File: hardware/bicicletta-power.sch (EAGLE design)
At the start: 19 parts, among them IC1 LM5017, IC2 LM1117-3.3

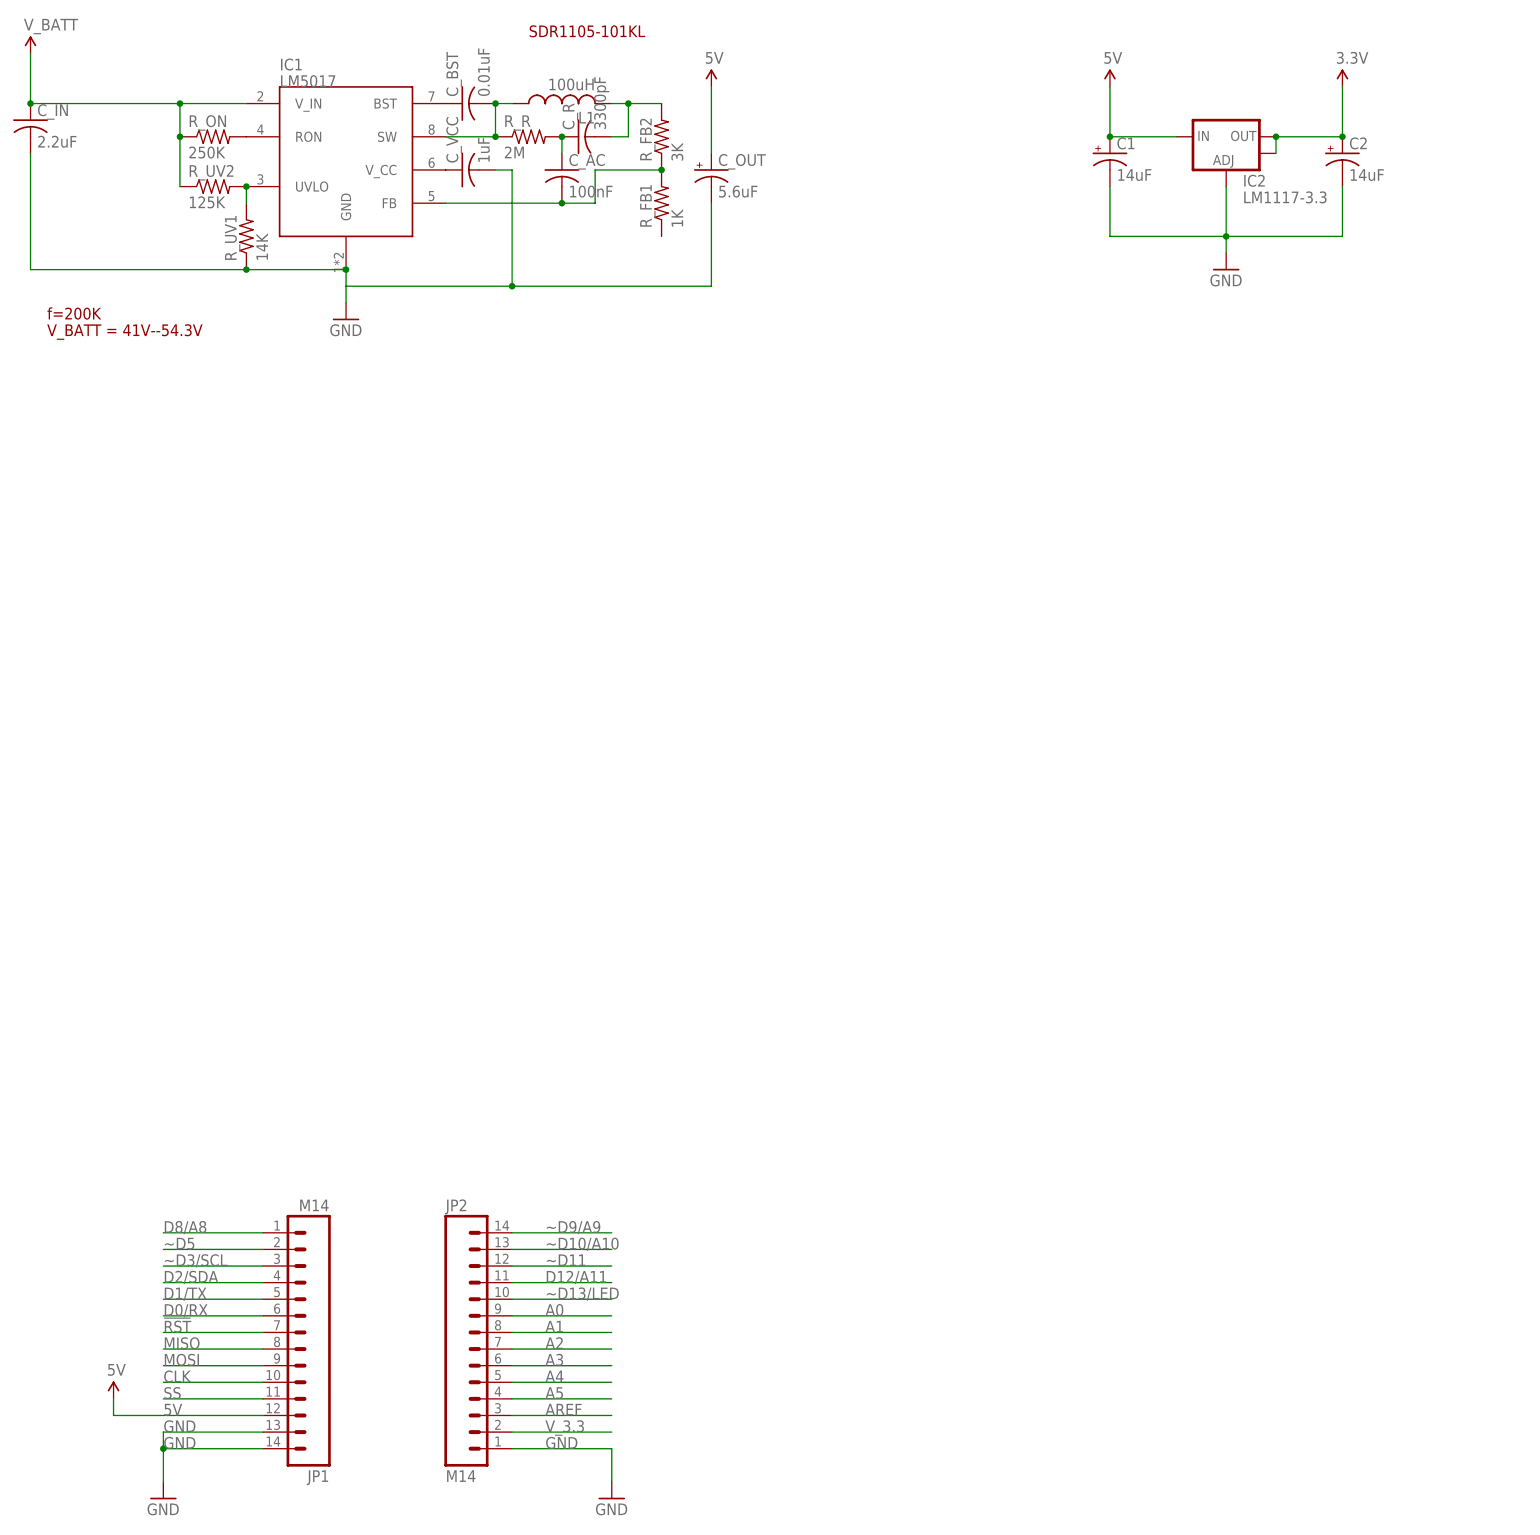
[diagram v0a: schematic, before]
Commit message: Adding connectors.
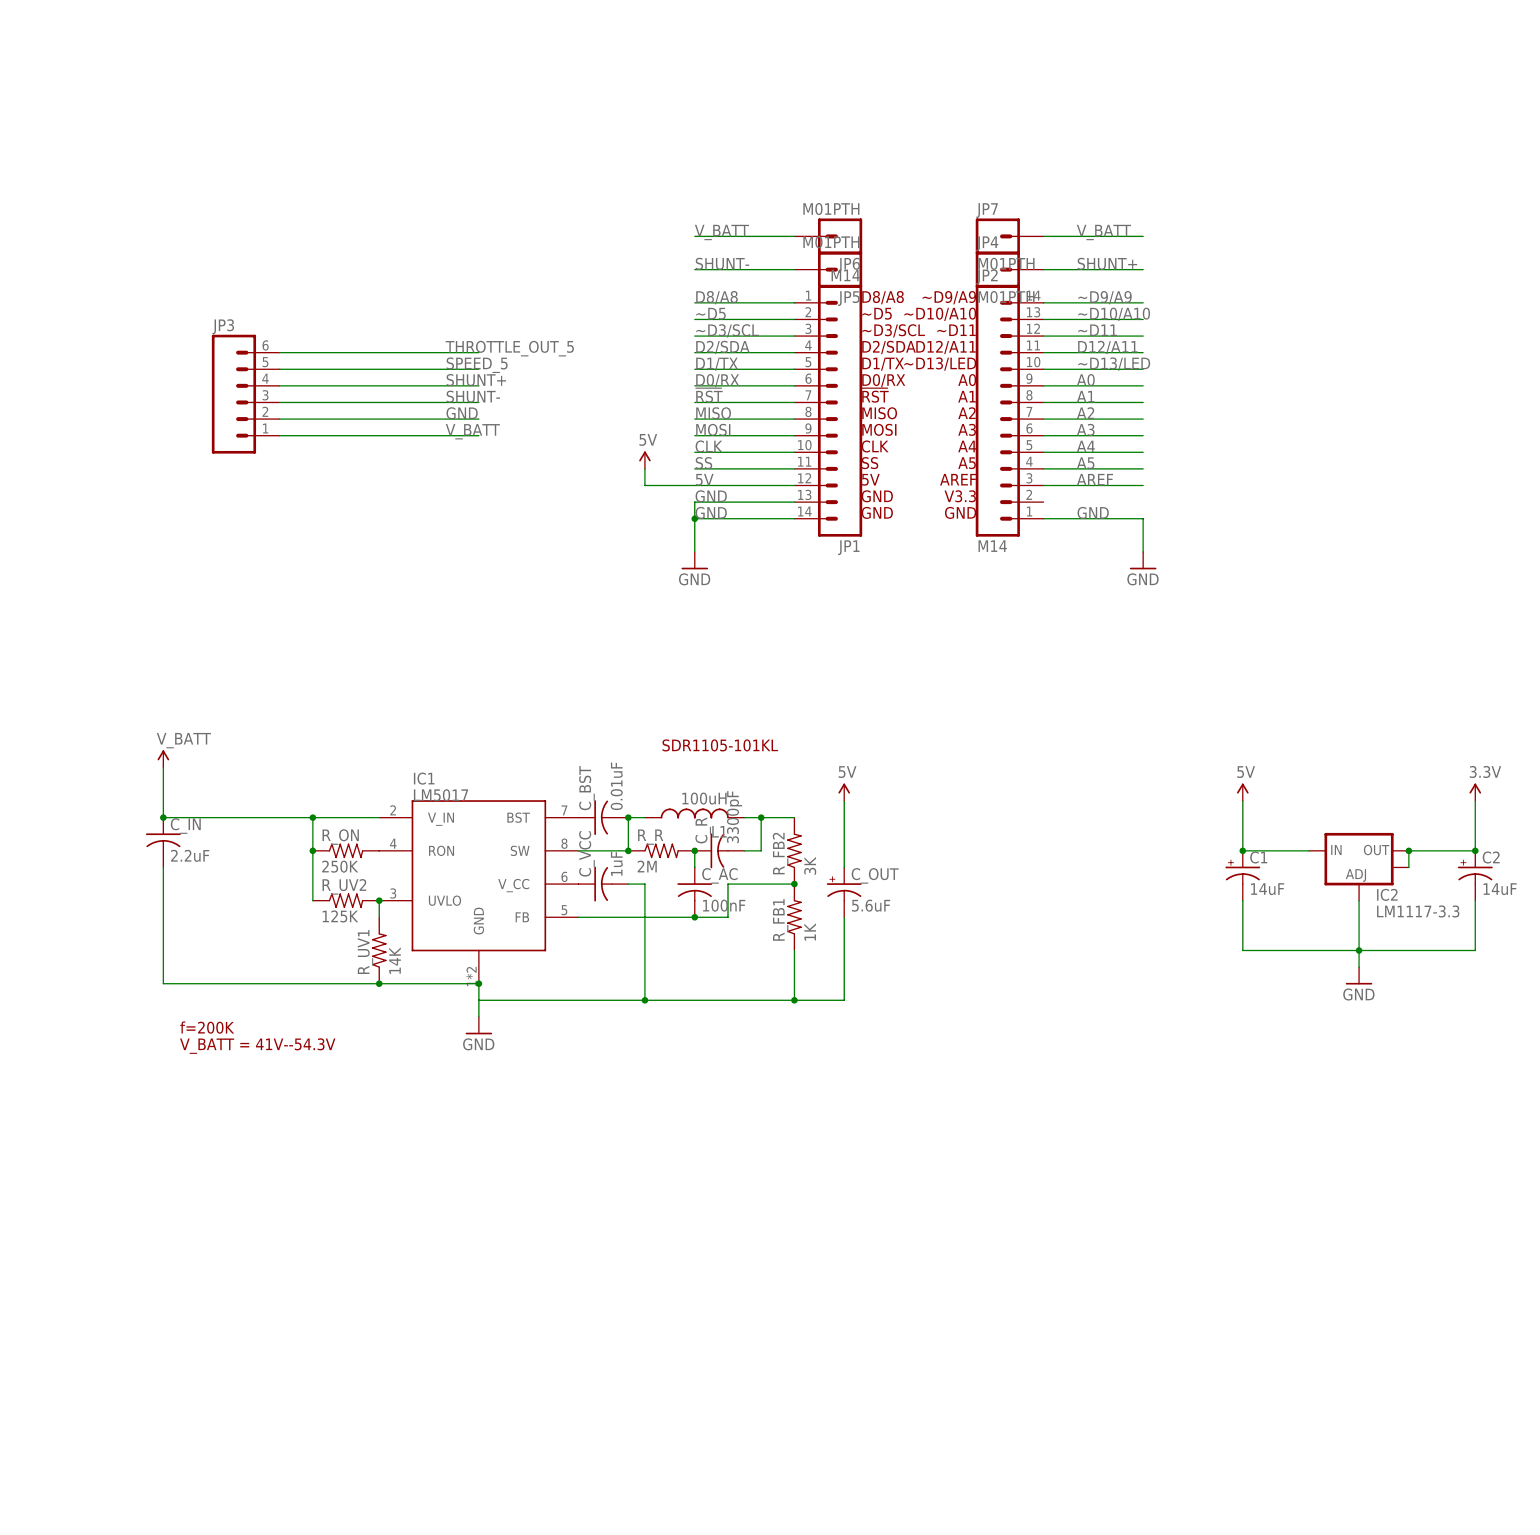
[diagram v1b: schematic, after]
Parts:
- added JP3: (no value), SparkFun-Connectors:M06LONGPADS
- added JP4, JP5, JP6, JP7: M01PTH, SparkFun-Connectors:M01PTH
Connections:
- removed net V_3.3: JP2.2
- new net SHUNT+: JP3.4, JP4.1
- new net SHUNT-: JP3.3
- new net SPEED_5: JP3.5
- new net THROTTLE_OUT_5: JP3.6
- net GND: now also JP3.2, R_FB1.1
- net V_BATT: now also JP3.1, JP6.1, JP7.1
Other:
- note added: "!RST"
- note added: "5V"
- note added: "A0"
- note added: "A1"
- note added: "A2"
- note added: "A3"
- note added: "A4"
- note added: "A5"
- note added: "AREF"
- note added: "CLK"
- note added: "D0/RX"
- note added: "D1/TX"
- note added: "D12/A11"
- note added: "D2/SDA"
- note added: "D8/A8"
- note added: "GND"
- note added: "MISO"
- note added: "MOSI"
- note added: "SS"
- note added: "V3.3"
- note added: "~D10/A10"
- note added: "~D11"
- note added: "~D13/LED"
- note added: "~D3/SCL"
- note added: "~D5"
- note added: "~D9/A9"
- moved on the sheet: C1, C2, C_AC, C_BST, C_IN, C_OUT, C_R, C_VCC, IC1, IC2, JP1, JP2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

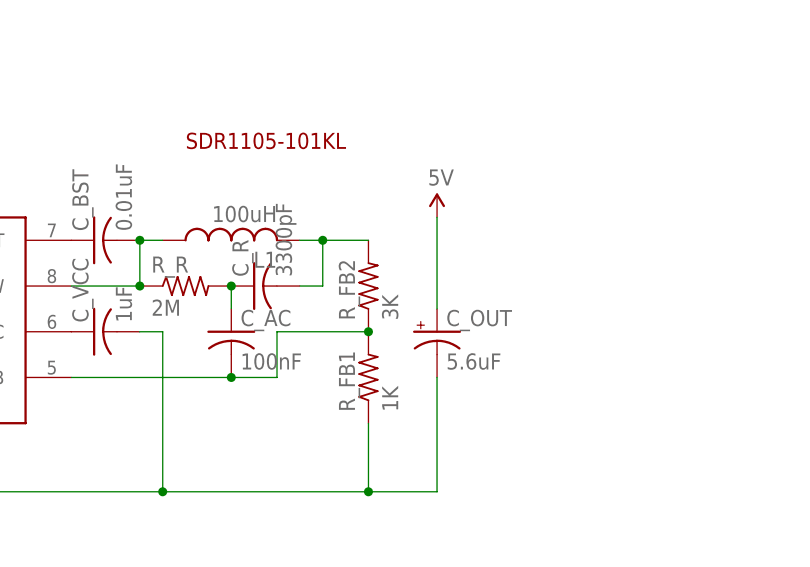
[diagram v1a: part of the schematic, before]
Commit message: Error in regulator connections. Please double check
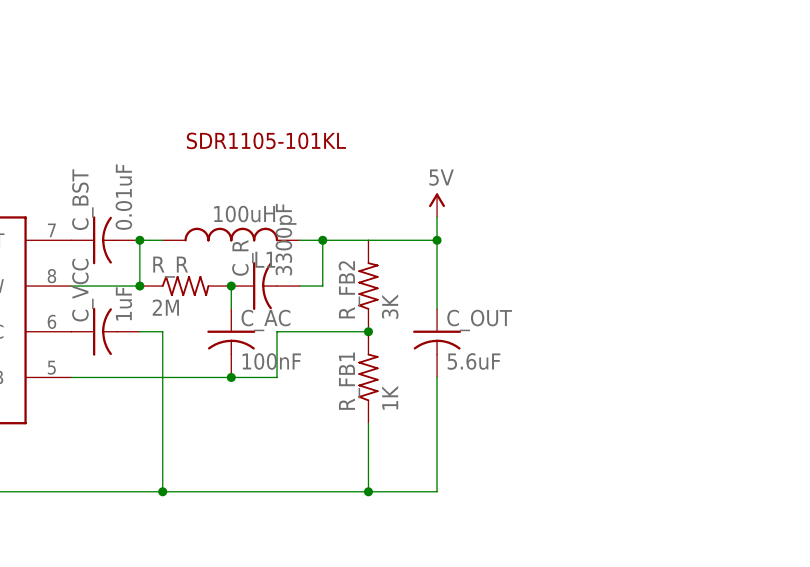
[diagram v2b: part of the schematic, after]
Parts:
- C_OUT: device rcl:CPOL-USUD-5X5,8 -> rcl:C-USC0603
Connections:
- removed net N$5: C_R.2, L1.2, R_FB2.2
- net 5V: now also C_OUT.1, C_R.2, L1.2, R_FB2.2; no longer C_OUT.+
- net GND: now also C_OUT.2; no longer C_OUT.-
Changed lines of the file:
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@@
 <part name="C_BST" library="rcl" deviceset="C-US" device="C0603" value="0.01uF"/>
 <part name="C_IN" library="rcl" deviceset="C-US" device="C1210K" value="2.2uF"/>
-<part name="C_OUT" library="rcl" deviceset="CPOL-US" device="UD-5X5,8" value="5.6uF"/>
+<part name="C_OUT" library="rcl" deviceset="C-US" device="C0603" value="5.6uF"/>
 <part name="R_UV2" library="rcl" deviceset="R-US_" device="M0805" value="125K"/>
 <part name="R_UV1" library="rcl" deviceset="R-US_" device="M0805" value="14K"/>
@@
 <pinref part="R_UV1" gate="G$1" pin="1"/>
 <junction x="60.96" y="109.22"/>
-<pinref part="C_OUT" gate="G$1" pin="-"/>
+<pinref part="C_OUT" gate="G$1" pin="2"/>
 <wire x1="76.2" y1="106.68" x2="101.6" y2="106.68" width="0.1524" layer="91"/>
 <wire x1="101.6" y1="106.68" x2="124.46" y2="106.68" width="0.1524" layer="91"/>
@@
 </segment>
 <segment>
-<pinref part="C_OUT" gate="G$1" pin="+"/>
+<pinref part="C_OUT" gate="G$1" pin="1"/>
 <pinref part="U$5" gate="G$1" pin="5V"/>
-<wire x1="132.08" y1="137.16" x2="132.08" y2="127" width="0.1524" layer="91"/>
+<wire x1="132.08" y1="137.16" x2="132.08" y2="134.62" width="0.1524" layer="91"/>
+<pinref part="L1" gate="G$1" pin="2"/>
+<pinref part="R_FB2" gate="G$1" pin="2"/>
+<wire x1="132.08" y1="134.62" x2="132.08" y2="127" width="0.1524" layer="91"/>
+<wire x1="116.84" y1="134.62" x2="119.38" y2="134.62" width="0.1524" layer="91"/>
+<pinref part="C_R" gate="G$1" pin="2"/>
+<wire x1="119.38" y1="134.62" x2="124.46" y2="134.62" width="0.1524" layer="91"/>
+<wire x1="116.84" y1="129.54" x2="119.38" y2="129.54" width="0.1524" layer="91"/>
+<wire x1="119.38" y1="129.54" x2="119.38" y2="134.62" width="0.1524" layer="91"/>
+<junction x="119.38" y="134.62"/>
+<wire x1="124.46" y1="134.62" x2="132.08" y2="134.62" width="0.1524" layer="91"/>
+<junction x="132.08" y="134.62"/>
 </segment>
 </net>
@@
 </segment>
 </net>
-<net name="N$5" class="0">
-<segment>
-<pinref part="L1" gate="G$1" pin="2"/>
-<pinref part="R_FB2" gate="G$1" pin="2"/>
-<wire x1="116.84" y1="134.62" x2="119.38" y2="134.62" width="0.1524" layer="91"/>
-<pinref part="C_R" gate="G$1" pin="2"/>
-<wire x1="119.38" y1="134.62" x2="124.46" y2="134.62" width="0.1524" layer="91"/>
-<wire x1="116.84" y1="129.54" x2="119.38" y2="129.54" width="0.1524" layer="91"/>
-<wire x1="119.38" y1="129.54" x2="119.38" y2="134.62" width="0.1524" layer="91"/>
-<junction x="119.38" y="134.62"/>
-</segment>
-</net>
